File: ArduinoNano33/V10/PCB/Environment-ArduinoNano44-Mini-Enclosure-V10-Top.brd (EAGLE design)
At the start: 145 x 219 mm, 78 parts, among them IC1 BME680, J4 QUIC, Q1 5.8A/30V/35mΩ, Q2 5.8A/30V/35mΩ

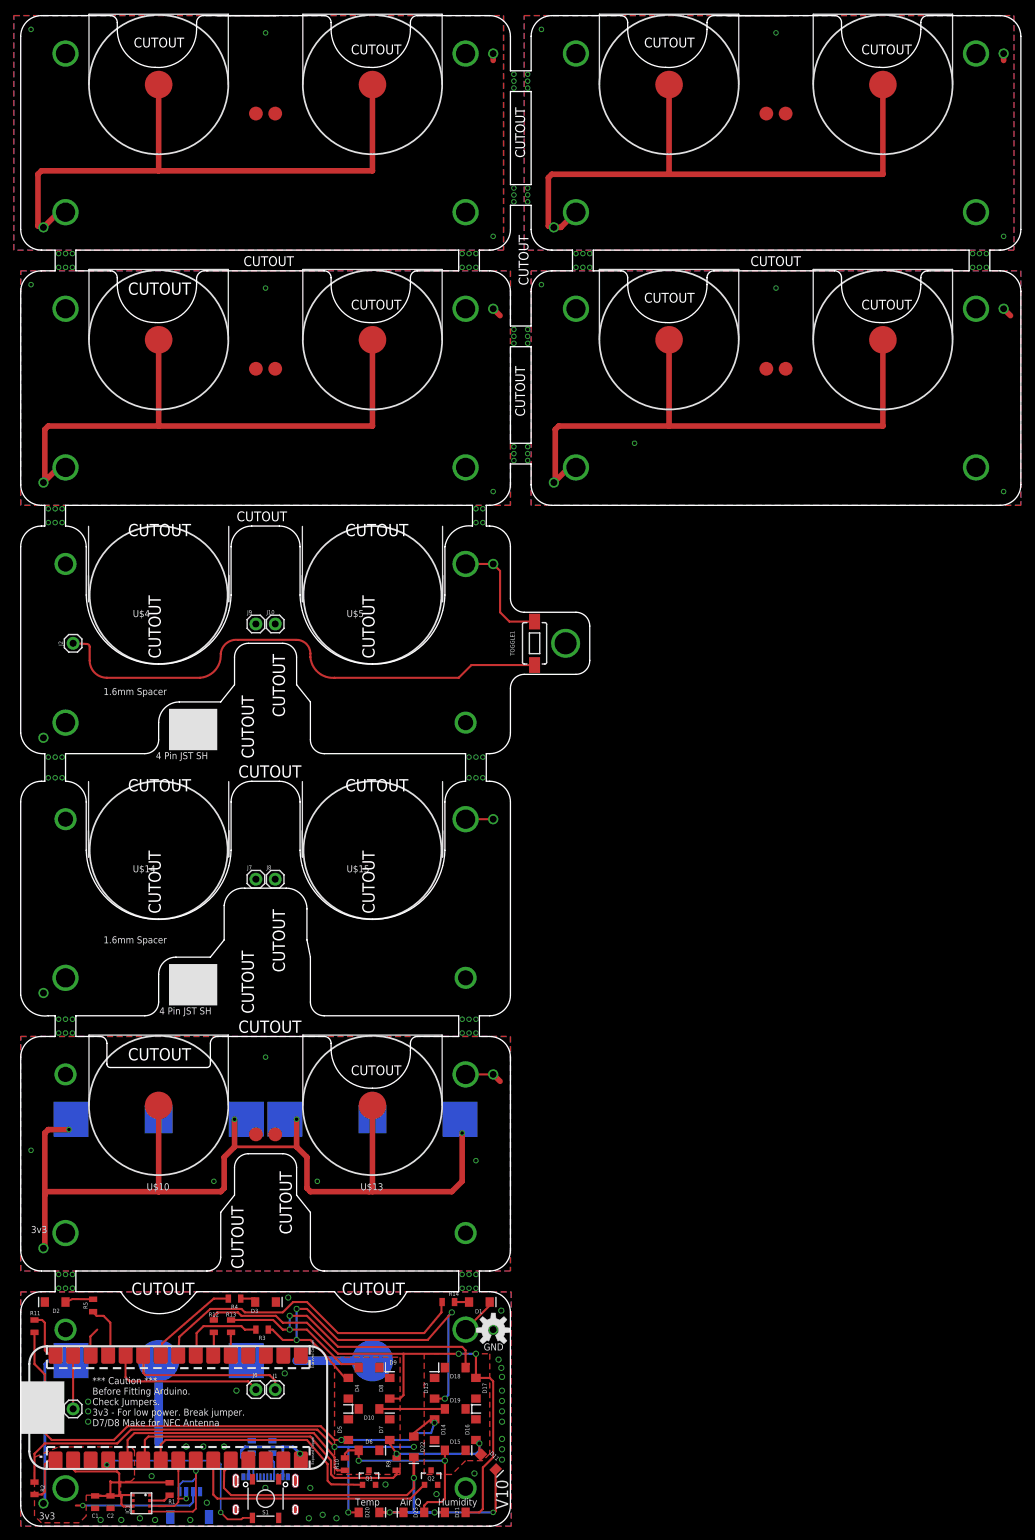
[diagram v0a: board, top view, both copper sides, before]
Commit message: Split out personal environmental sensor boards into individual Eagle files.
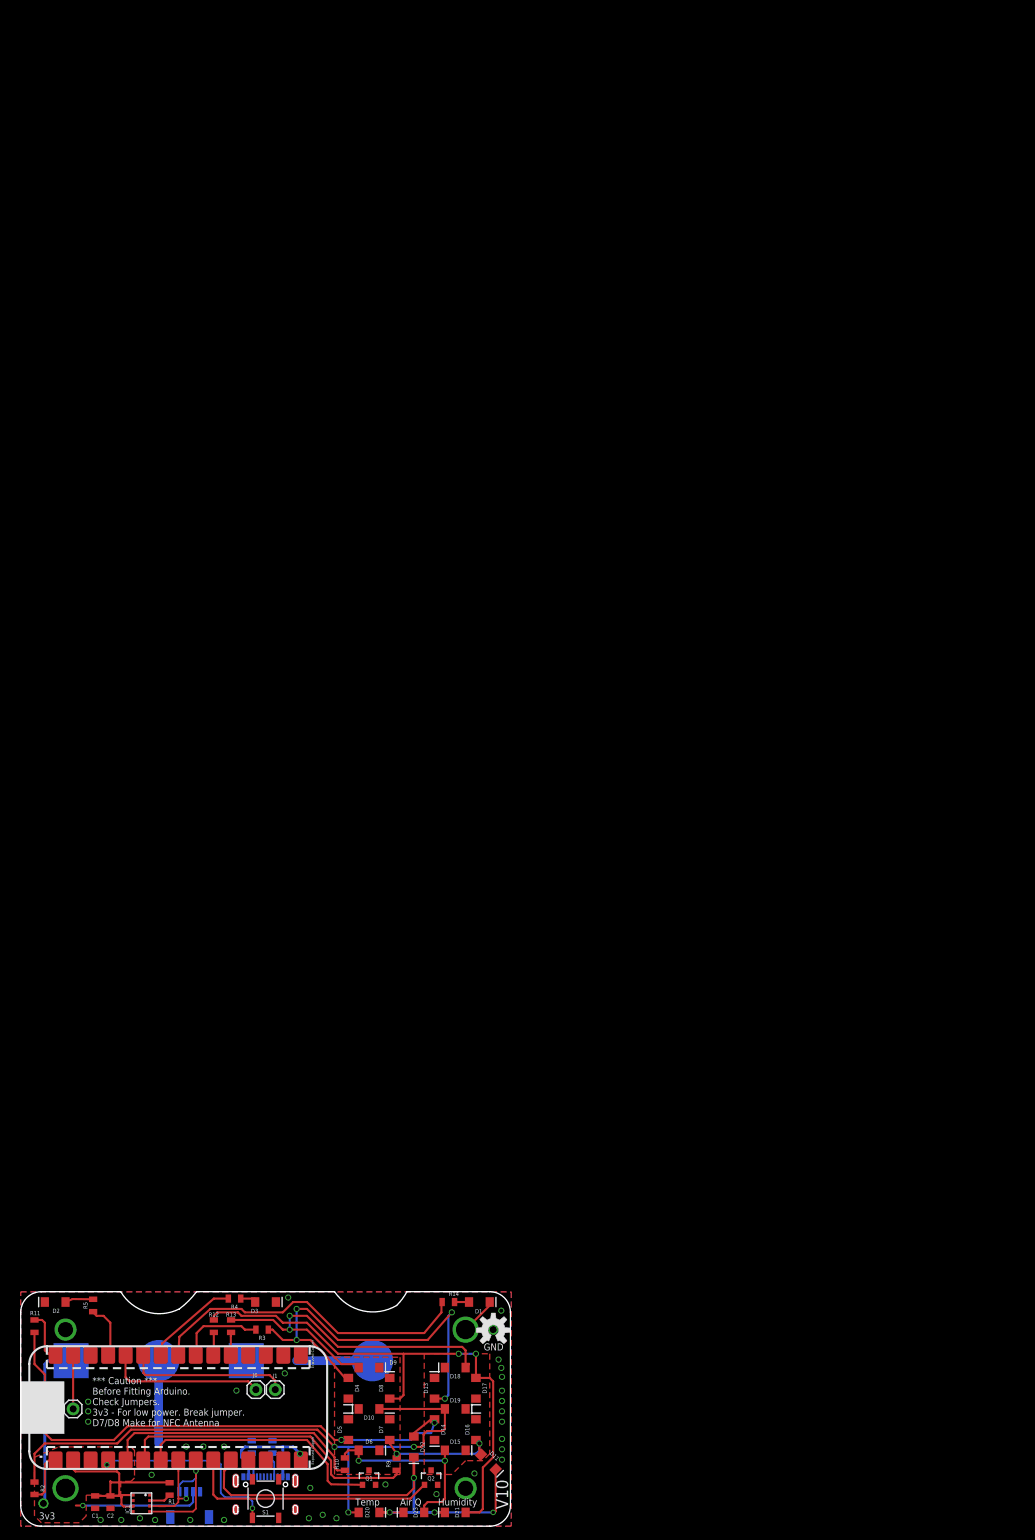
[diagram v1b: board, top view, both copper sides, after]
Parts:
- removed J10, J2, J7, J8, J9: (no value), SparkFun-Connectors:1X01
- removed LOGO2, LOGO3, LOGO5, LOGO6: OSHW-LOGOL, SparkFun-Aesthetics:OSHW-LOGO-L
- removed LOGO7: OSHW-LOGOM, SparkFun-Aesthetics:OSHW-LOGO-M
- removed TOGGLE1: MOMENTARY-SWITCH-SPST-SMD-6.0X3.5MM, ThingySticks:TACTILE_SWITCH_SMD_6.0X3.5MM
- removed U$10, U$11, U$12, U$13, U$16, U$17, U$18, U$19, U$20, U$7: CR2032-SPLIT-PCB-POSITIVE, ThingySticks:CR2032-SMD-POSITIVE-TERMINAL
- removed U$14, U$15, U$4, U$5: CR2032-SPLIT-PCB-MIDDLE, ThingySticks:CR2032-SMD-MIDDLE-OUTLINE
- removed U$2, U$3: (no value), ThingySticks:CR2032-SMD
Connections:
- removed net D+: J5.A6, J5.B6
- removed net D-: J5.A7, J5.B7
- removed net SHIELD: J5.SHLD1, J5.SHLD2, J5.SHLD3, J5.SHLD4, J5.SHLD5, J5.SHLD6, J5.SHLD7, J5.SHLD8
- net 3.3V: no longer U$10.+, U$11.+, U$12.+, U$13.+, U$16.+, U$17.+, U$18.+, U$19.+, U$2.+$1, U$2.+$2, U$20.+, U$3.+$1, U$3.+$2, U$7.+
- net A0: no longer J2.1, TOGGLE1.1
- net GND: no longer TOGGLE1.2, U$2.-, U$3.-
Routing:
- net 3.3V: track 564.6 -> 74.2 mm, vias 20 -> 3
- net A0: track 105.4 -> 29.4 mm
- net GND: track 59.7 -> 28.4 mm, vias 85 -> 38
- net G: track 82.1 -> 91.4 mm
- net SWITCH1: track 4.12 -> 0.06 mm
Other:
- board size 145 x 219 mm -> 71 x 34 mm
- board text removed: "1.6mm PCB"
- board text removed: "1.6mm Spacer"
- board text removed: "1mm PCB"
- board text removed: "4 Pin JST SH"
- board text removed: "Battary + this side"
- board text removed: "Bottom PCB"
- board text removed: "CR2032"
- board text removed: "CUTOUT"
- board text removed: "Chris"
- board text removed: "Coin Cell Base Option"
- board text removed: "Dan"
- board text removed: "Dan SmartSpaces Custom Name Base"
- board text removed: "Do not fit batteries when on external power"
- board text removed: "Environment Sensor"
- board text removed: "Github.com/ThingySticks/PersonalEnvironmentSensor"
- board text removed: "Keychain Middle. Bottom wall slightly smaller to allow for a cover to slide on using the grove"
- board text removed: "Middle PCB"
- board text removed: "Personal Environment Sensor"
- board text removed: "SmartSpaces"
- board text removed: "ThingySticks"
- board text removed: "ThingySticks Custom Name Base"
- board text removed: "ThingySticks.Com"
- board text removed: "Wilson"
